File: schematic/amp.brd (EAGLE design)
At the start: 47.9 x 30.5 mm, 22 parts, among them IC1 LM386N-1, Q1 2SK117, SW1 MCS10B, SW2 MCS10B

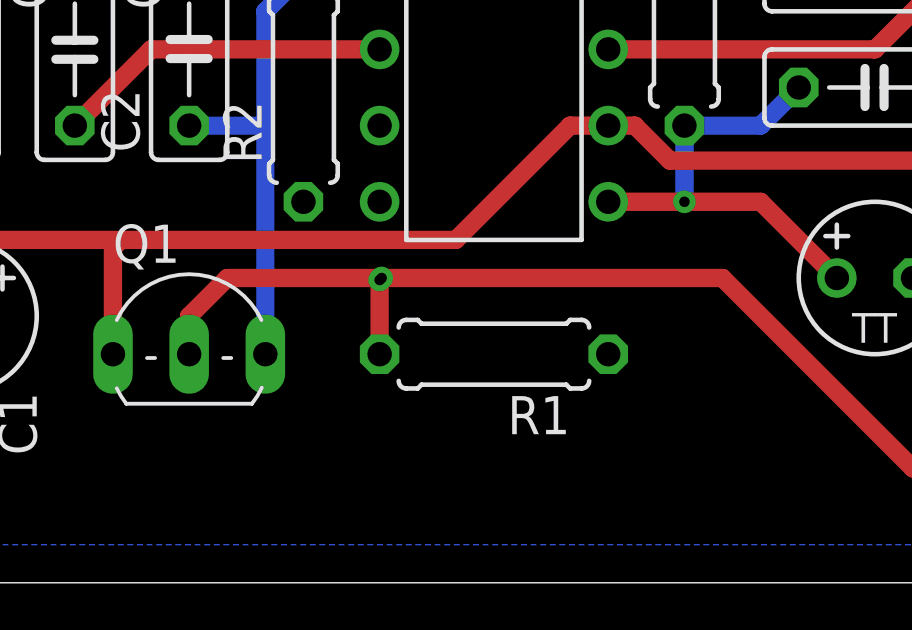
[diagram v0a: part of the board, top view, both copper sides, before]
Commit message: Remove stray via.
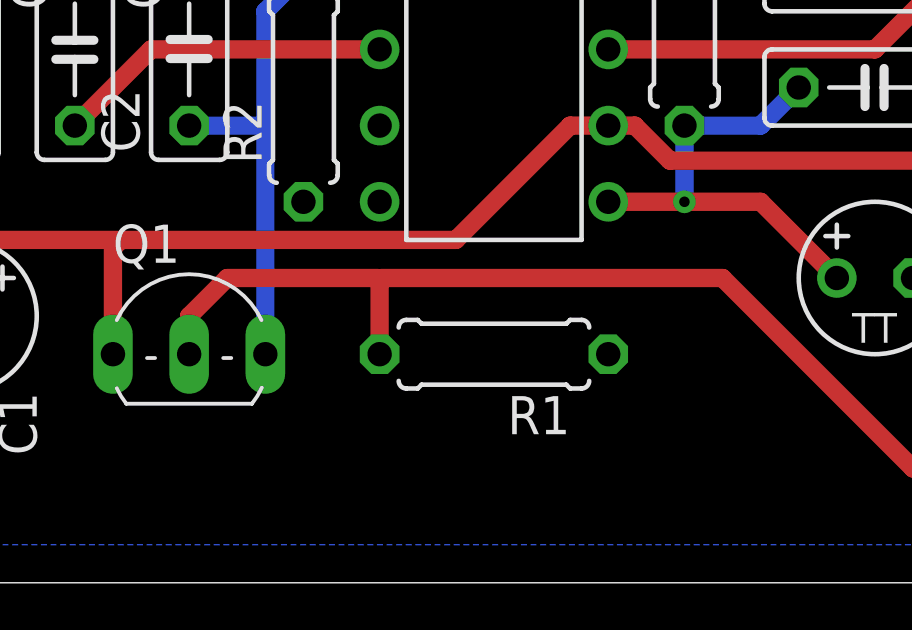
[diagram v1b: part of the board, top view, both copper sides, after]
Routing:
- net N$1: track 37.5 -> 37.4 mm, vias 2 -> 0
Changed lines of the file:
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@@
 <layer number="17" name="Pads" color="2" fill="1" visible="yes" active="yes"/>
 <layer number="18" name="Vias" color="2" fill="1" visible="yes" active="yes"/>
-<layer number="19" name="Unrouted" color="6" fill="1" visible="no" active="yes"/>
+<layer number="19" name="Unrouted" color="6" fill="1" visible="yes" active="yes"/>
 <layer number="20" name="Dimension" color="15" fill="1" visible="no" active="yes"/>
 <layer number="21" name="tPlace" color="7" fill="1" visible="no" active="yes"/>
@@
 <wire x1="43.18" y1="54.61" x2="36.83" y2="54.61" width="0.6096" layer="1"/>
 <wire x1="36.83" y1="54.61" x2="30.48" y2="60.96" width="0.6096" layer="1"/>
-<wire x1="19.116540625" y1="60.96" x2="30.48" y2="60.96" width="0.6096" layer="1"/>
-<wire x1="19.116540625" y1="60.96" x2="13.97" y2="60.96" width="0.6096" layer="1"/>
-<wire x1="13.97" y1="60.96" x2="12.7" y2="59.69" width="0.6096" layer="1"/>
+<wire x1="12.7" y1="59.69" x2="13.97" y2="60.96" width="0.6096" layer="1"/>
 <wire x1="12.7" y1="59.69" x2="12.7" y2="58.42" width="0.6096" layer="1"/>
-<wire x1="19.05" y1="58.42" x2="19.05" y2="60.893459375" width="0.6096" layer="1"/>
-<wire x1="19.05" y1="60.893459375" x2="19.116540625" y2="60.96" width="0.6096" layer="16"/>
-<via x="19.116540625" y="60.96" extent="1-16" drill="0.35"/>
-<via x="19.05" y="60.893459375" extent="1-16" drill="0.35"/>
+<wire x1="19.05" y1="60.893459375" x2="19.05" y2="58.42" width="0.6096" layer="1"/>
+<wire x1="13.97" y1="60.96" x2="18.983459375" y2="60.96" width="0.6096" layer="1"/>
+<wire x1="18.983459375" y1="60.96" x2="19.05" y2="60.893459375" width="0.6096" layer="1"/>
+<wire x1="30.48" y1="60.96" x2="19.116540625" y2="60.96" width="0.6096" layer="1"/>
+<wire x1="19.116540625" y1="60.96" x2="19.05" y2="60.893459375" width="0.6096" layer="1"/>
 </signal>
 <signal name="GND">
